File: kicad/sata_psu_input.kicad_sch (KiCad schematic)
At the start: 6 parts, among them J8 12V DC 8-10A, Q8 AOD4185

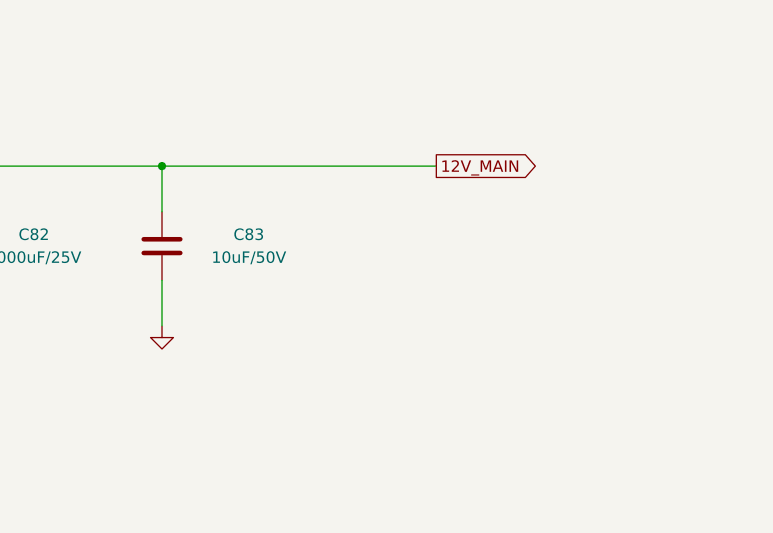
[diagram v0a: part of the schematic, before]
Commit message: v2: per-port 5V buck with 0R neighbour sharing, plus rail indicators
Every port now has its own local 5V node and its own buck footprint, with
adjacent nodes joined by 0R links (R61-R64). How a port gets its 5V is a
populate choice rather than a layout one -- BUCKS/LINKS at the top of
gen_sch.py is the whole configuration, and the lands are always present.

This closes v1's largest open issue. One 3A TPS563200 was under-rated
against a five-bay 5V rail; capping a buck at a three-port group makes its
worst case 2.1A and the same part is correctly sized.

Indicators: one 12V LED on the common rail, tapped after Q8 so it also
proves the reverse-polarity guard conducts, and one 5V LED per port on the
local node at the header, so it lights whether that port's 5V came from its
own buck or across a link.

verify.py gains check 5, the rail populate rules. A DNP part is still a
wire in the netlist, so a build that fits R63 with both U2 and U4 populated
passes ERC and netlist equivalence and parallels two regulators on the
bench. Nothing else can catch it. It also refuses groups over three ports
and any link carrying more than one port's current.

Also fixed: check_layout.py reported "0 symbols checked" and PASSED after
KiCad re-saved the sheets in its own format, because text[text.find(m):]
yields the last character rather than "" when the marker is absent, so the
`or text` fallback never fired. It now fails loudly when it parses nothing.

Schematic verified (ERC clean, 50 nets equivalent to the independent SKiDL
description, pins match pads). Board placed at 64.9 x 76.0 mm, 112 parts,
0 DRC violations. Routing still not started.

Co-Authored-By: Claude Opus 5 <noreply@anthropic.com>
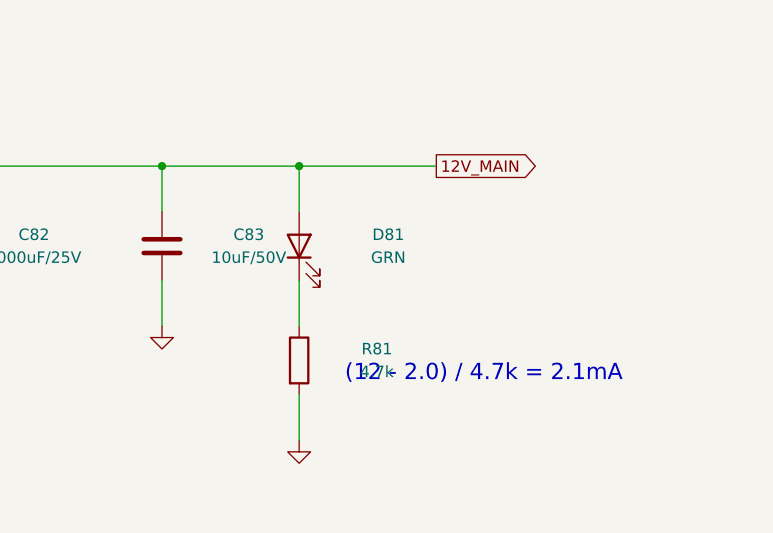
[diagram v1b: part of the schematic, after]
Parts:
- added D81: GRN, LED_SMD:LED_0603_1608Metric, symbol Device:LED
- added R81: 4.7k, Resistor_SMD:R_0603_1608Metric, symbol Device:R
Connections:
- net 12V_MAIN: now also D81.2 (A)
- net GND: now also R81.2
- new net: D81.1 (K), R81.1
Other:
- note added: "(12 - 2.0) / 4.7k = 2.1mA"
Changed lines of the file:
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@@
   )
   (wire
-    (pts (xy 170.18 60.96) (xy 200.66 60.96))
+    (pts (xy 170.18 60.96) (xy 185.42 60.96))
+    (stroke (width 0) (type default))
+  )
+  (wire
+    (pts (xy 185.42 60.96) (xy 200.66 60.96))
     (stroke (width 0) (type default))
   )
@@
   (wire
     (pts (xy 170.18 73.66) (xy 170.18 78.74))
+    (stroke (width 0) (type default))
+  )
+  (wire
+    (pts (xy 185.42 60.96) (xy 185.42 66.04))
+    (stroke (width 0) (type default))
+  )
+  (wire
+    (pts (xy 185.42 73.66) (xy 185.42 78.74))
+    (stroke (width 0) (type default))
+  )
+  (wire
+    (pts (xy 185.42 86.36) (xy 185.42 91.44))
     (stroke (width 0) (type default))
   )
@@
     (diameter 0) (color 0 0 0 0)
   )
+  (junction
+    (at 185.42 60.96)
+    (diameter 0) (color 0 0 0 0)
+  )
   (global_label "12V_MAIN"
     (shape output)
@@
     (at 38.1 34.29 0)
     (effects (font (size 2.54 2.54)) (justify left bottom))
+  )
+  (text "(12 - 2.0) / 4.7k = 2.1mA"
+    (exclude_from_sim no)
+    (at 190.5 85.09 0)
+    (effects (font (size 1.8 1.8)) (justify left bottom))
   )
   (text "Star ground: single point back to the brick negative"
@@
   )
   (symbol
+    (lib_id "Device:LED")
+    (at 185.42 69.85 90)
+    (unit 1)
+    (exclude_from_sim no)
+    (in_bom yes)
+    (on_board yes)
+    (dnp no)
+    (fields_autoplaced yes)
+    (property "Reference" "D81" (at 195.326 68.58 90) (effects (font (size 1.27 1.27))))
+    (property "Value" "GRN" (at 195.326 71.11999999999999 90) (effects (font (size 1.27 1.27))))
+    (property "Footprint" "LED_SMD:LED_0603_1608Metric" (at 185.42 69.85 0) (effects (font (size 1.27 1.27)) (hide yes)))
+    (property "Datasheet" "~" (at 185.42 69.85 0) (effects (font (size 1.27 1.27)) (hide yes)))
+    (instances
+      (project "sata_psu"
+        (path "/f0e190f0-6b7d-5633-94d7-0d3d9757c179/ccf6d1e6-c4ae-5b40-a4c1-2315706323bf"
+          (reference "D81") (unit 1)
+        )
+      )
+    )
+  )
+  (symbol
+    (lib_id "Device:R")
+    (at 185.42 82.55 0)
+    (unit 1)
+    (exclude_from_sim no)
+    (in_bom yes)
+    (on_board yes)
+    (dnp no)
+    (fields_autoplaced yes)
+    (property "Reference" "R81" (at 194.05599999999998 81.28 0) (effects (font (size 1.27 1.27))))
+    (property "Value" "4.7k" (at 194.05599999999998 83.82 0) (effects (font (size 1.27 1.27))))
+    (property "Footprint" "Resistor_SMD:R_0603_1608Metric" (at 185.42 82.55 0) (effects (font (size 1.27 1.27)) (hide yes)))
+    (property "Datasheet" "~" (at 185.42 82.55 0) (effects (font (size 1.27 1.27)) (hide yes)))
+    (instances
+      (project "sata_psu"
+        (path "/f0e190f0-6b7d-5633-94d7-0d3d9757c179/ccf6d1e6-c4ae-5b40-a4c1-2315706323bf"
+          (reference "R81") (unit 1)
+        )
+      )
+    )
+  )
+  (symbol
+    (lib_id "power:GND")
+    (at 185.42 91.44 0)
+    (unit 1)
+    (exclude_from_sim no)
+    (in_bom no)
+    (on_board no)
+    (dnp no)
+    (fields_autoplaced yes)
+    (property "Reference" "#PWR0114" (at 185.42 88.89999999999999 0) (effects (font (size 1.27 1.27)) (hide yes)))
+    (property "Value" "GND" (at 185.42 96.52000000000001 0) (effects (font (size 1.27 1.27)) (hide yes)))
+    (property "Footprint" "" (at 185.42 91.44 0) (effects (font (size 1.27 1.27)) (hide yes)))
+    (property "Datasheet" "~" (at 185.42 91.44 0) (effects (font (size 1.27 1.27)) (hide yes)))
+    (instances
+      (project "sata_psu"
+        (path "/f0e190f0-6b7d-5633-94d7-0d3d9757c179/ccf6d1e6-c4ae-5b40-a4c1-2315706323bf"
+          (reference "#PWR0114") (unit 1)
+        )
+      )
+    )
+  )
+  (symbol
     (lib_id "power:PWR_FLAG")
     (at 78.74 86.36 0)
@@
     (dnp no)
     (fields_autoplaced yes)
-    (property "Reference" "#FLG0112" (at 87.376 85.09 0) (effects (font (size 1.27 1.27)) (hide yes)))
+    (property "Reference" "#FLG0115" (at 87.376 85.09 0) (effects (font (size 1.27 1.27)) (hide yes)))
     (property "Value" "PWR_FLAG" (at 87.376 87.63 0) (effects (font (size 1.27 1.27)) (hide yes)))
     (property "Footprint" "" (at 78.74 86.36 0) (effects (font (size 1.27 1.27)) (hide yes)))
@@
       (project "sata_psu"
         (path "/f0e190f0-6b7d-5633-94d7-0d3d9757c179/ccf6d1e6-c4ae-5b40-a4c1-2315706323bf"
-          (reference "#FLG0112") (unit 1)
+          (reference "#FLG0115") (unit 1)
         )
       )
@@
     (dnp no)
     (fields_autoplaced yes)
-    (property "Reference" "#PWR0113" (at 87.63 90.17 0) (effects (font (size 1.27 1.27)) (hide yes)))
+    (property "Reference" "#PWR0116" (at 87.63 90.17 0) (effects (font (size 1.27 1.27)) (hide yes)))
     (property "Value" "GND" (at 87.63 92.71 0) (effects (font (size 1.27 1.27)) (hide yes)))
     (property "Footprint" "" (at 78.74 91.44 0) (effects (font (size 1.27 1.27)) (hide yes)))
@@
       (project "sata_psu"
         (path "/f0e190f0-6b7d-5633-94d7-0d3d9757c179/ccf6d1e6-c4ae-5b40-a4c1-2315706323bf"
-          (reference "#PWR0113") (unit 1)
-        )
-      )
+          (reference "#PWR0116") (unit 1)
+        )
+      )
